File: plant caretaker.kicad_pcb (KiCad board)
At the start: 2 copper layers, 56 parts, among them J3 Water_Pump, J4 Kitronik, J5 694106402002, Q1 FDMS86255, U1 UDA1380HN_N2, U2 TMP175AIDR, U4 LM2596S-5, U5 PAM8403D, U6 ESP32_C3_ZERO

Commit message: Part of PCB
Dziękuję Maciej :*
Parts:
- added LS1: Speaker, Connector_PinHeader_1.27mm:PinHeader_1x02_P1.27mm_Vertical_SMD_Pin1Left, F.Cu at (151.8, 67.9)
- added LS2: Speaker, Connector_PinHeader_1.27mm:PinHeader_1x02_P1.27mm_Vertical_SMD_Pin1Left, F.Cu at (145.8, 74.3)
- C10, C23, C24, R12, R6, R9, U1: moved to B.Cu
- FB2: value FerriteBead -> FB
- J3: footprint Connector_PinHeader_1.00mm:PinHeader_1x02_P1.00mm_Vertical_SMD_Pin1Right -> Connector_PinHeader_1.27mm:PinHeader_1x02_P1.27mm_Vertical_SMD_Pin1Left
- J4: footprint Connector_PinHeader_1.00mm:PinHeader_1x03_P1.00mm_Vertical_SMD_Pin1Left -> Connector_PinHeader_1.27mm:PinHeader_1x03_P1.27mm_Vertical_SMD_Pin1Left
- moved C2 75.1 mm to (77.6, 40.6)
- moved R3 72.9 mm to (86.5, 83.2)
- moved R2 72.7 mm to (86.5, 85.3)
- moved R1 72.7 mm to (86.5, 87.0)
- moved C3 61.7 mm to (97.8, 89.1)
- moved U2 56.5 mm to (92.1, 85.1)
- moved U4 50.5 mm to (70.3, 59.1)
- moved C1 44.5 mm to (93.3, 60.3)
- moved J4 37.2 mm to (120.4, 41.9)
- moved C11 36.2 mm to (103.1, 103.0)
- moved C14 36.2 mm to (103.1, 108.0)
- moved C17 36.2 mm to (107.1, 103.0)
- moved FB2 35.2 mm to (132.1, 59.7), turned to -90 degrees
- moved U6 34.9 mm to (135.3, 31.8)
- moved C21 32.7 mm to (125.7, 74.9), turned to -90 degrees
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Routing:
- net +3V3: track 0.00 -> 58.2 mm, vias 0 -> 5
- net GND: track 0.00 -> 46.9 mm, vias 0 -> 8
- net /AudioCodec/SCL: track 0.00 -> 44.2 mm, vias 0 -> 1
- net /AudioAmplifier/MUTE_IN: track 0.00 -> 43.7 mm, vias 0 -> 2
- net /AudioCodec/SDA: track 0.00 -> 43.5 mm, vias 0 -> 1
- net /AudioAmplifier/SHDN_IN: track 0.00 -> 36.7 mm, vias 0 -> 2
- net Net-(U1-VOUTR): track 0.00 -> 33.5 mm, vias 0 -> 3
- net /AudioCodec/VDDA(DA): track 0.00 -> 25.8 mm, vias 0 -> 1
- net Net-(U6-3V3_OUT): track 0.00 -> 24.8 mm
- net Net-(C9-Pad1): track 0.00 -> 17.8 mm
- net /AudioCodec/A1: track 0.00 -> 17.4 mm, vias 0 -> 2
- net /AudioCodec/VADCP: track 0.00 -> 15.6 mm, vias 0 -> 1
- net Net-(U5-LOUT+): track 0.00 -> 15.6 mm
- net /CODEC.BCKI: track 0.00 -> 15.1 mm, vias 0 -> 1
- net /AudioCodec/VDDD: track 0.00 -> 14.3 mm, vias 0 -> 1
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
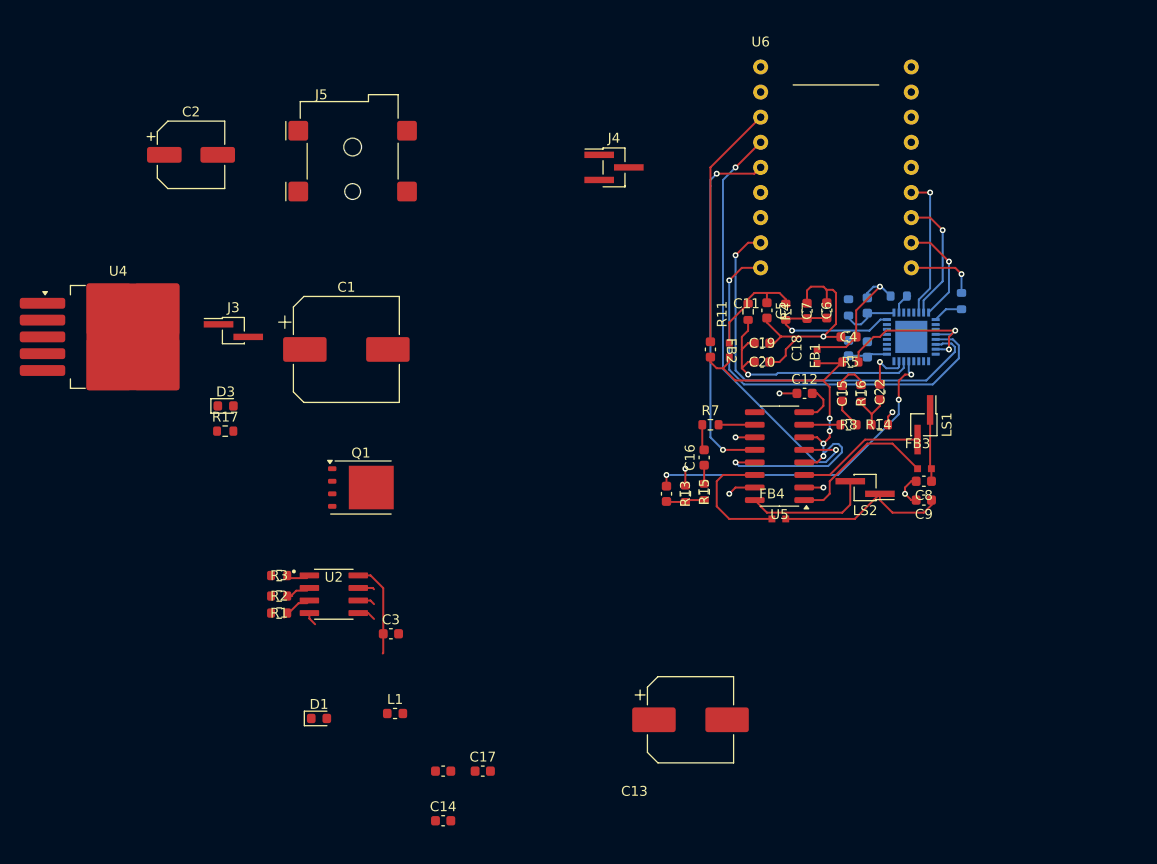
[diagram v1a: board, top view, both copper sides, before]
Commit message: Added few components to PCB
:)
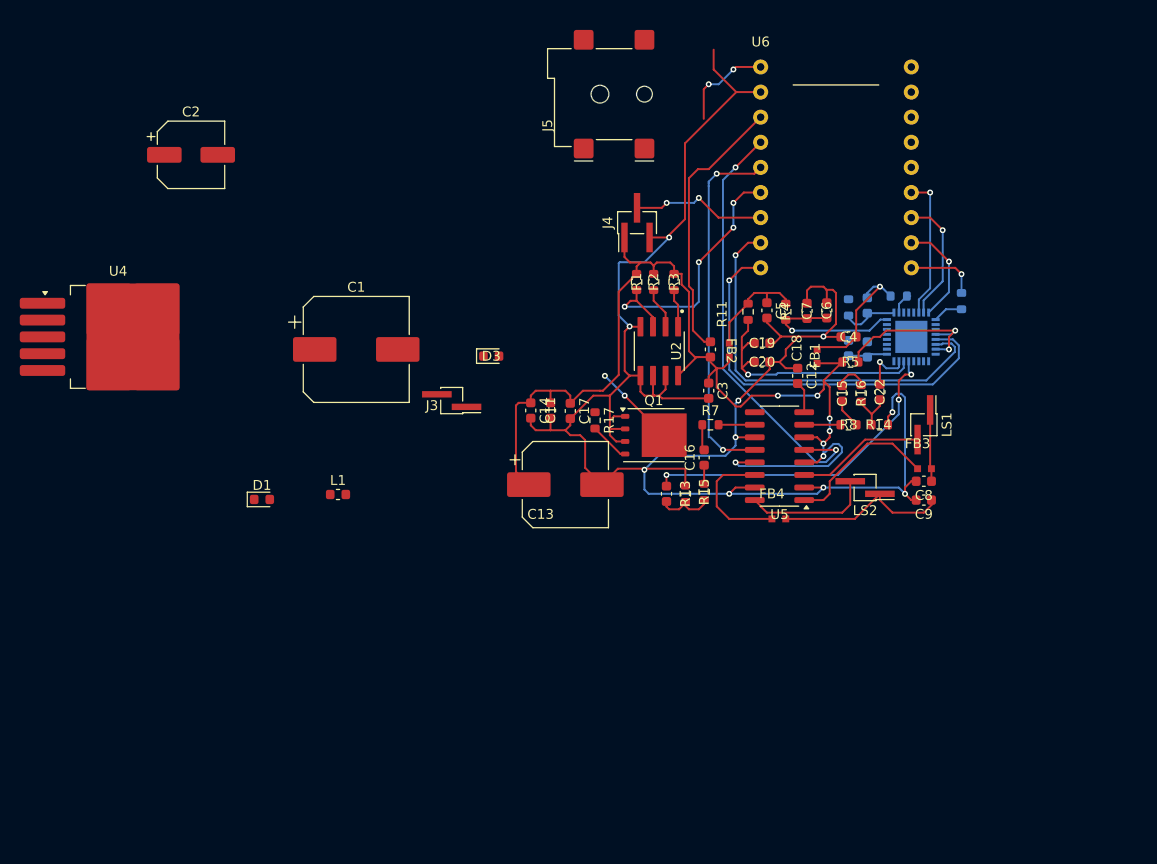
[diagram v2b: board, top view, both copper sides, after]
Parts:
- moved R3 49.8 mm to (126.5, 53.5), turned to -90 degrees
- moved R2 49.4 mm to (124.4, 53.5), turned to -90 degrees
- moved R1 49.3 mm to (122.7, 53.5), turned to -90 degrees
- moved C14 42.4 mm to (112.0, 66.5), turned to -90 degrees
- moved U2 41.1 mm to (125.0, 60.5), turned to -90 degrees
- moved C3 40.5 mm to (130.0, 64.5), turned to -90 degrees
- moved C11 38.1 mm to (114.0, 66.5), turned to -90 degrees
- moved C17 37.5 mm to (116.0, 66.5), turned to -90 degrees
- moved R17 37.4 mm to (118.5, 67.5), turned to -90 degrees
- moved Q1 30.1 mm to (124.5, 69.0)
- moved D3 27.3 mm to (108.0, 61.0)
- moved J5 27.3 mm to (120.4, 34.5), turned to 90 degrees
- moved C13 26.9 mm to (115.5, 74.0)
- moved J3 23.2 mm to (104.0, 65.5), turned to 180 degrees
- moved D1 22.9 mm to (84.8, 75.5)
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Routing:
- net GND: track 46.9 -> 204.6 mm, vias 8 -> 10
- net +3V3: track 58.2 -> 113.4 mm, vias 5 -> 7
- net /TempSensor/ALERT: track 2.94 -> 28.2 mm, vias 0 -> 4
- net Net-(J4-Pin_2): track 0.00 -> 13.7 mm, vias 0 -> 2
- net /BuckConverter/5V_OUT: track 0.00 -> 9.69 mm, vias 0 -> 2
- net Net-(D3-A): track 0.00 -> 8.70 mm, vias 0 -> 2
- net Net-(Q1-G): track 0.00 -> 4.12 mm
- net Net-(U6-3V3_OUT): track 24.8 -> 27.6 mm
- net Net-(C21-Pad2): track 3.91 -> 6.31 mm
- net /AudioCodec/SCL: track 44.2 -> 45.8 mm
- net /AudioCodec/SDA: track 43.5 -> 45.0 mm
- net Net-(U5-VREF): track 4.24 -> 3.17 mm

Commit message: All elements are connected
:)
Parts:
- U4: moved to B.Cu
- moved U4 44.3 mm to (106.5, 33.6), turned to 90 degrees
- moved C2 34.8 mm to (105.5, 61.5)
- moved D1 30.4 mm to (103.5, 51.5)
- moved L1 23.7 mm to (103.5, 54.0)
- moved C1 20.6 mm to (113.0, 51.5)
- moved D3 11.5 mm to (119.5, 61.0), turned to -90 degrees
- moved J3 11.1 mm to (114.5, 62.0)
- moved R17 8.14 mm to (120.0, 75.5), turned to 90 degrees
- moved C23 4.19 mm to (140.0, 60.8)
- moved C24 4.07 mm to (142.0, 60.8)
- moved C13 3.50 mm to (112.0, 74.0)
- moved C4 2.69 mm to (145.0, 56.5), turned to -90 degrees
- moved FB4 2.66 mm to (133.7, 77.5)
- moved R6 0.45 mm to (144.0, 56.5)
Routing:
- net GND: track 204.6 -> 329.6 mm, vias 10 -> 22
- net /BuckConverter/PWM_IN: track 0.00 -> 80.5 mm, vias 0 -> 2
- net /BuckConverter/5V_OUT: track 9.69 -> 72.1 mm
- net Net-(D3-K): track 0.00 -> 53.9 mm, vias 0 -> 1
- net /AudioCodec/SCL: track 45.8 -> 67.6 mm, vias 1 -> 3
- net Net-(D1-K): track 0.00 -> 20.8 mm, vias 0 -> 1
- net /AudioCodec/SDA: track 45.0 -> 62.1 mm, vias 1 -> 3
- net /AudioCodec/VDDD: track 14.3 -> 22.5 mm, vias 1 -> 2
- net Net-(Q1-G): track 4.12 -> 9.99 mm, vias 0 -> 2
- net Net-(D3-A): track 8.70 -> 13.3 mm
- net /AudioCodec/VREF: track 4.07 -> 8.34 mm
- net Net-(U5-ROUT-): track 12.8 -> 10.1 mm
- net Net-(C9-Pad1): track 17.8 -> 20.4 mm
- net /AudioCodec/A1: track 17.4 -> 18.4 mm
- net /AudioCodec/VDDA(DA): track 25.8 -> 26.8 mm
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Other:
- board outline added: 56.5 x 52 mm

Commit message: Changed a little
:)
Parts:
- moved J5 1.58 mm to (120.5, 36.1), turned to 180 degrees
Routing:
- net Net-(D3-K): track 53.9 -> 66.1 mm, vias 1 -> 3
- net /BuckConverter/5V_OUT: track 72.1 -> 76.8 mm
- net GND: track 329.6 -> 332.7 mm
- net Net-(J4-Pin_2): track 13.7 -> 14.6 mm

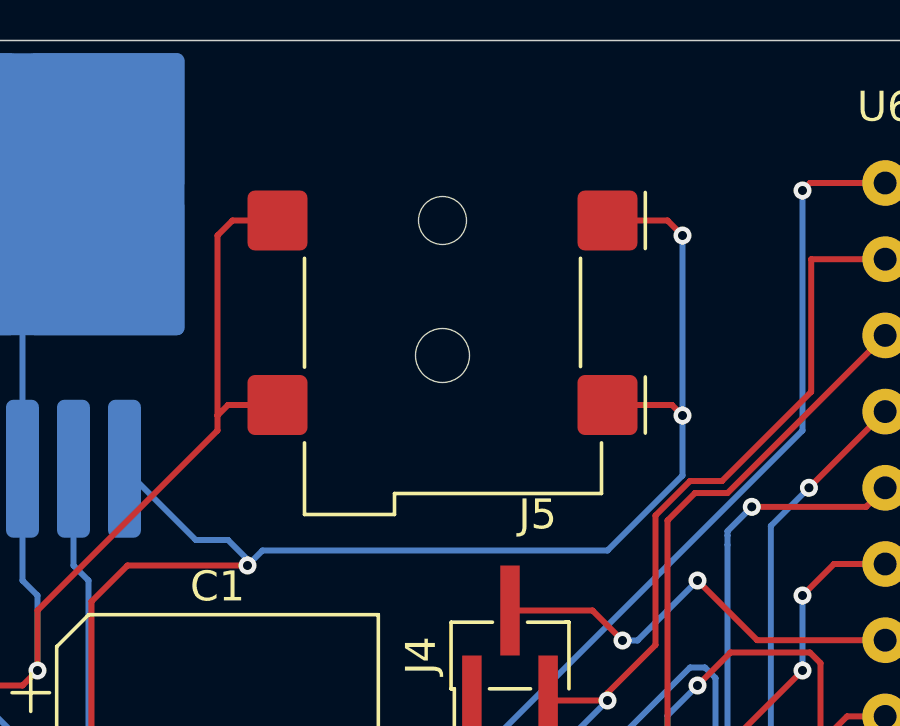
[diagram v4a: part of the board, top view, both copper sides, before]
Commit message: I moved one component
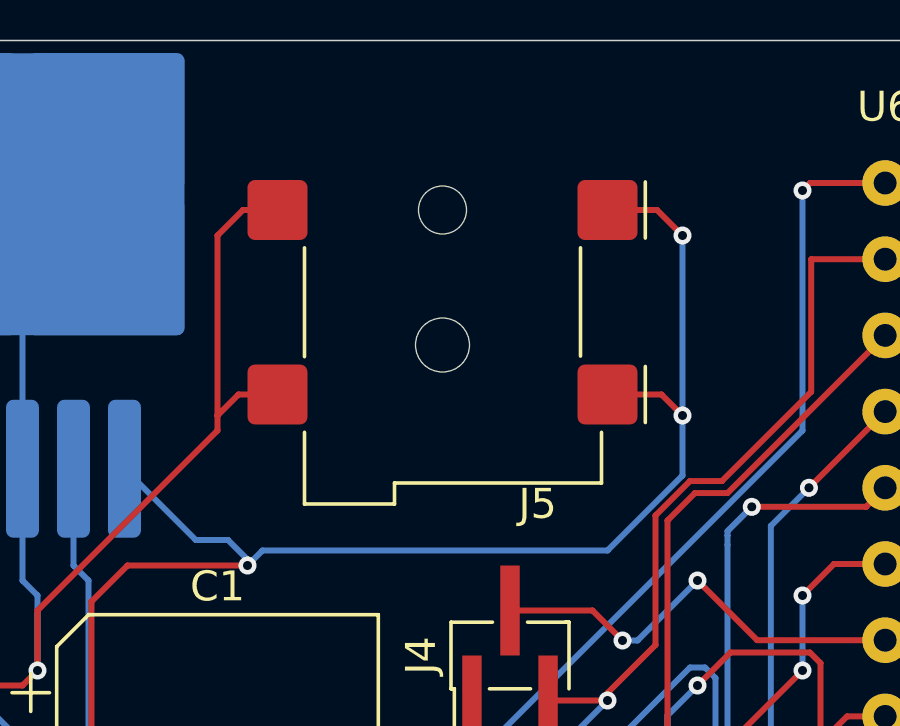
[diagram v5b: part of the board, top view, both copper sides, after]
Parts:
- moved J5 0.35 mm to (120.5, 35.7)
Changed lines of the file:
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@@
 	(footprint "Connector_BarrelJack:BarrelJack_Wuerth_694106106102_2.0x5.5mm"
 		(layer "F.Cu")
-		(at 120.5 36.075 180)
+		(at 120.5 35.725 180)
 		(descr "Wuerth Elektronik 694106106102 Barrel Jack, 2.0x5.5mm, https://www.we-online.com/components/products/datasheet/694106106102.pdf")
 		(tags "barrel jack Wuerth Elektronik 694106106102")
@@
 	)
 	(segment
-		(start 127.6 42.834314)
-		(end 127.6 47.15)
+		(start 107 46)
+		(end 107 48)
 		(width 0.2)
 		(layer "F.Cu")
@@
 	)
 	(segment
-		(start 113 40)
-		(end 107 46)
+		(start 127.6 42.834314)
+		(end 127.6 47.15)
 		(width 0.2)
 		(layer "F.Cu")
@@
 	)
 	(segment
+		(start 115 38.8)
+		(end 113.7 38.8)
+		(width 0.2)
+		(layer "F.Cu")
+		(net 1)
+	)
+	(segment
 		(start 120.405 67.095)
 		(end 120 67.5)
@@
 	)
 	(segment
-		(start 113 33.5)
-		(end 113 39.5)
-		(width 0.2)
-		(layer "F.Cu")
-		(net 1)
-	)
-	(segment
 		(start 109 68)
 		(end 109.5 68.5)
@@
 	)
 	(segment
-		(start 113.35 39.15)
-		(end 113 39.5)
-		(width 0.2)
-		(layer "F.Cu")
-		(net 1)
-	)
-	(segment
 		(start 142.5 59)
 		(end 143.5 59)
@@
 	)
 	(segment
-		(start 115 39.15)
-		(end 113.35 39.15)
-		(width 0.2)
-		(layer "F.Cu")
-		(net 1)
-	)
-	(segment
 		(start 142.875 54.61)
 		(end 143 54.5)
@@
 	)
 	(segment
-		(start 113.5 33)
-		(end 113 33.5)
-		(width 0.2)
-		(layer "F.Cu")
-		(net 1)
-	)
-	(segment
 		(start 141.945 55.6)
 		(end 141.945 54.315)
@@
 	)
 	(segment
-		(start 115 33)
-		(end 113.5 33)
-		(width 0.2)
-		(layer "F.Cu")
-		(net 1)
-	)
-	(segment
 		(start 120 67.5)
 		(end 120 65)
@@
 	)
 	(segment
-		(start 113 39.5)
-		(end 113 40)
+		(start 122 63)
+		(end 122.03 62.97)
 		(width 0.2)
 		(layer "F.Cu")
@@
 	)
 	(segment
-		(start 122 63)
-		(end 122.03 62.97)
+		(start 113.7 38.8)
+		(end 113 39.5)
 		(width 0.2)
 		(layer "F.Cu")
@@
 	)
 	(segment
+		(start 113 39.5)
+		(end 113 40)
+		(width 0.2)
+		(layer "F.Cu")
+		(net 1)
+	)
+	(segment
 		(start 124.02 49)
 		(end 126 49)
@@
 	)
 	(segment
-		(start 107 46)
-		(end 107 48)
-		(width 0.2)
-		(layer "F.Cu")
-		(net 1)
-	)
-	(segment
 		(start 149.86 74.93)
 		(end 149.86 74.295)
@@
 	)
 	(segment
+		(start 113 40)
+		(end 107 46)
+		(width 0.2)
+		(layer "F.Cu")
+		(net 1)
+	)
+	(segment
 		(start 132.715 74.295)
 		(end 132.08 74.93)
@@
 	)
 	(segment
+		(start 113.85 32.65)
+		(end 113 33.5)
+		(width 0.2)
+		(layer "F.Cu")
+		(net 1)
+	)
+	(segment
 		(start 155.54 57.54)
 		(end 155.54 59.96)
@@
 	)
 	(segment
+		(start 115 32.65)
+		(end 113.85 32.65)
+		(width 0.2)
+		(layer "F.Cu")
+		(net 1)
+	)
+	(segment
 		(start 135.89 57.6)
 		(end 135.89 57.15)
@@
 	)
 	(segment
+		(start 113 33.5)
+		(end 113 39.5)
+		(width 0.2)
+		(layer "F.Cu")
+		(net 1)
+	)
+	(segment
 		(start 137.795 60.325)
 		(end 139.065 59.055)
@@
 	)
 	(segment
-		(start 128.15 39.15)
-		(end 128.5 39.5)
+		(start 127.65 32.65)
+		(end 128.5 33.5)
 		(width 0.2)
 		(layer "F.Cu")
@@
 	)
 	(segment
-		(start 128 33)
-		(end 128.5 33.5)
+		(start 126 38.8)
+		(end 127.8 38.8)
 		(width 0.2)
 		(layer "F.Cu")
@@
 	)
 	(segment
-		(start 114.5 59)
-		(end 113 60.5)
+		(start 127.8 38.8)
+		(end 128.5 39.5)
 		(width 0.2)
 		(layer "F.Cu")
@@
 	)
 	(segment
-		(start 113 60.5)
-		(end 113 61.365)
+		(start 126 32.65)
+		(end 127.65 32.65)
 		(width 0.2)
 		(layer "F.Cu")
@@
 	)
 	(segment
-		(start 110.5 58)
-		(end 110 58)
+		(start 114.5 59)
+		(end 113 60.5)
 		(width 0.2)
 		(layer "F.Cu")
@@
 	)
 	(segment
-		(start 126 33)
-		(end 128 33)
+		(start 113 60.5)
+		(end 113 61.365)
 		(width 0.2)
 		(layer "F.Cu")
@@
 	)
 	(segment
-		(start 110 44.5)
-		(end 114 44.5)
+		(start 110.5 58)
+		(end 110 58)
 		(width 0.2)
 		(layer "F.Cu")
@@
 	)
 	(segment
-		(start 126 39.15)
-		(end 128.15 39.15)
+		(start 110 44.5)
+		(end 114 44.5)
 		(width 0.2)
 		(layer "F.Cu")

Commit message: Changes
:)
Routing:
- net GND: track 333.0 -> 332.3 mm
- net /CODEC.DATAI: track 10.6 -> 11.2 mm
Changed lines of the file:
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@@
 	)
 	(segment
-		(start 141.605 59.02)
-		(end 142.125 58.5)
-		(width 0.2)
-		(layer "F.Cu")
-		(net 1)
-	)
-	(segment
 		(start 113 39.5)
 		(end 113 40)
@@
 	)
 	(segment
-		(start 145.91 56.655)
-		(end 145.67 56.895)
+		(start 146.05 56.655)
+		(end 146.205 56.5)
 		(width 0.2)
 		(layer "B.Cu")
@@
 	)
 	(segment
-		(start 145.415 57.785)
-		(end 144.46 57.785)
+		(start 145.91 56.655)
+		(end 145.67 56.895)
 		(width 0.2)
 		(layer "B.Cu")
@@
 	)
 	(segment
-		(start 148.6786 56.655)
-		(end 148.7424 56.5912)
+		(start 145.415 57.785)
+		(end 144.46 57.785)
 		(width 0.2)
 		(layer "B.Cu")
@@
 	)
 	(segment
+		(start 146.205 56.5)
+		(end 148.6512 56.5)
+		(width 0.2)
+		(layer "B.Cu")
+		(net 10)
+	)
+	(segment
 		(start 146.05 57.15)
 		(end 145.415 57.785)
@@
 	)
 	(segment
-		(start 146.05 56.655)
-		(end 148.6786 56.655)
+		(start 148.6512 56.5)
+		(end 148.7424 56.5912)
 		(width 0.2)
 		(layer "B.Cu")
@@
 	)
 	(segment
-		(start 152.4 49.53)
-		(end 154.305 51.435)
+		(start 153.4 49.53)
+		(end 154.305 50.435)
 		(width 0.2)
 		(layer "F.Cu")
@@
 	(segment
 		(start 150.495 49.53)
-		(end 152.4 49.53)
+		(end 153.4 49.53)
+		(width 0.2)
+		(layer "F.Cu")
+		(net 40)
+	)
+	(segment
+		(start 154.305 50.435)
+		(end 154.305 51.435)
 		(width 0.2)
 		(layer "F.Cu")
@@
 	)
 	(segment
+		(start 152.99 46.99)
+		(end 150.495 46.99)
+		(width 0.2)
+		(layer "F.Cu")
+		(net 44)
+	)
+	(segment
 		(start 153.67 48.26)
-		(end 152.4 46.99)
+		(end 153.67 47.67)
 		(width 0.2)
 		(layer "F.Cu")
@@
 	)
 	(segment
-		(start 152.4 46.99)
-		(end 150.495 46.99)
+		(start 153.67 47.67)
+		(end 152.99 46.99)
 		(width 0.2)
 		(layer "F.Cu")

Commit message: Perfection (maybe not)
:)
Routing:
- net GND: track 332.3 -> 332.9 mm

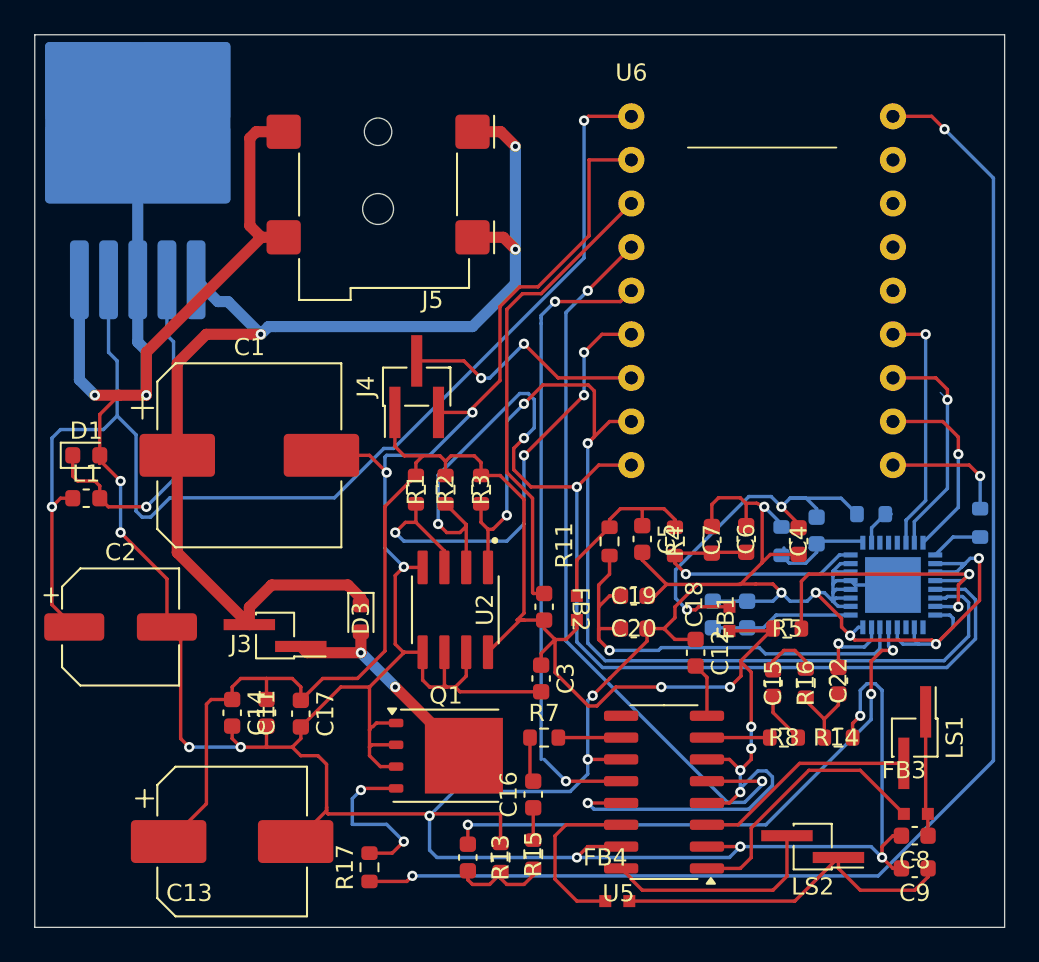
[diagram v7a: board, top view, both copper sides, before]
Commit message: Changed the size and place of the silkscreens
:)
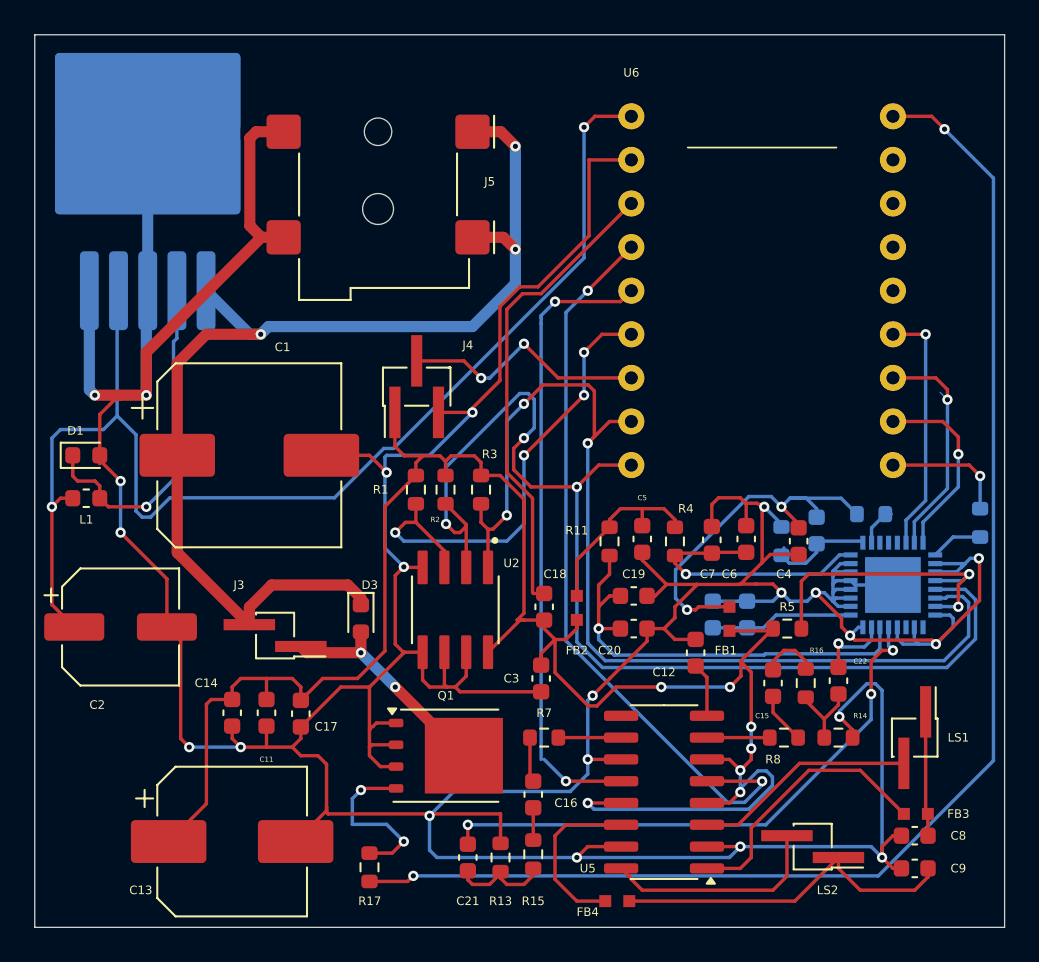
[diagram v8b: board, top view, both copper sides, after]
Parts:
- moved U4 0.86 mm to (107.1, 34.3)
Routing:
- net /BuckConverter/5V_OUT: track 76.8 -> 73.8 mm
- net GND: track 332.9 -> 331.9 mm
- net Net-(D3-K): track 66.1 -> 65.2 mm
- net Net-(D1-K): track 20.7 -> 20.0 mm
- net /AudioCodec/VDDA(DA): track 26.8 -> 26.1 mm
- net /AudioCodec/SCL: track 67.6 -> 66.9 mm
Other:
- copper layers 2 -> 4
